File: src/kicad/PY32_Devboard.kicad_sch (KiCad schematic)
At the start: 19 parts, among them J2 Micro_SD_Card, J5 Conn_01x09, J6 Conn_01x09, SW1 RESET, SW2 BOOT, SW3 RESET, SW4 BOOT, U1 CH340N, U2 ME6211A33M3G-N, U3 PY32F002BF15P6TR

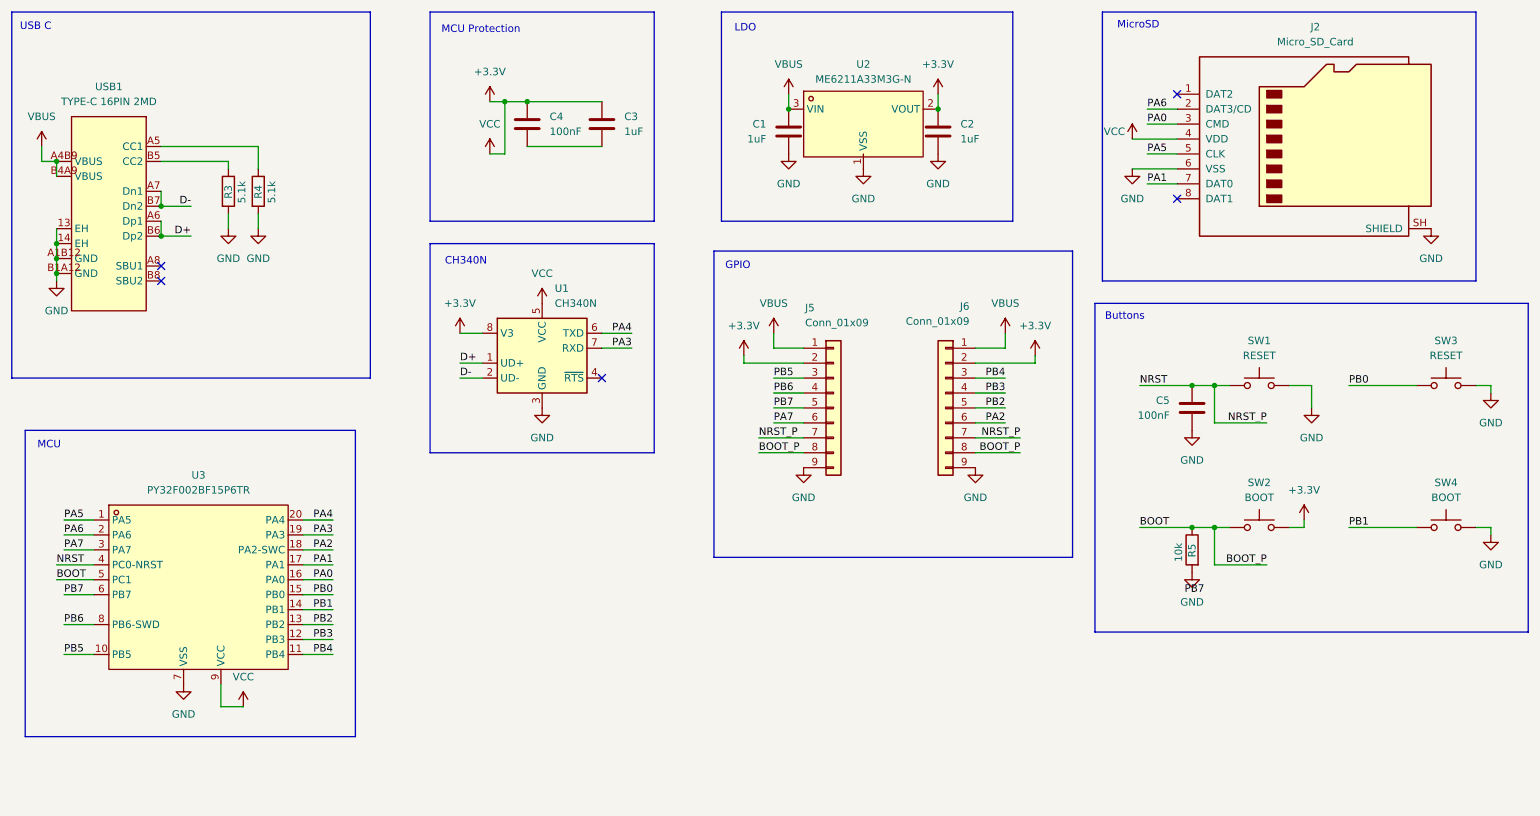
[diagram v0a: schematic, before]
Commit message: Changed Github For Fixed PCB
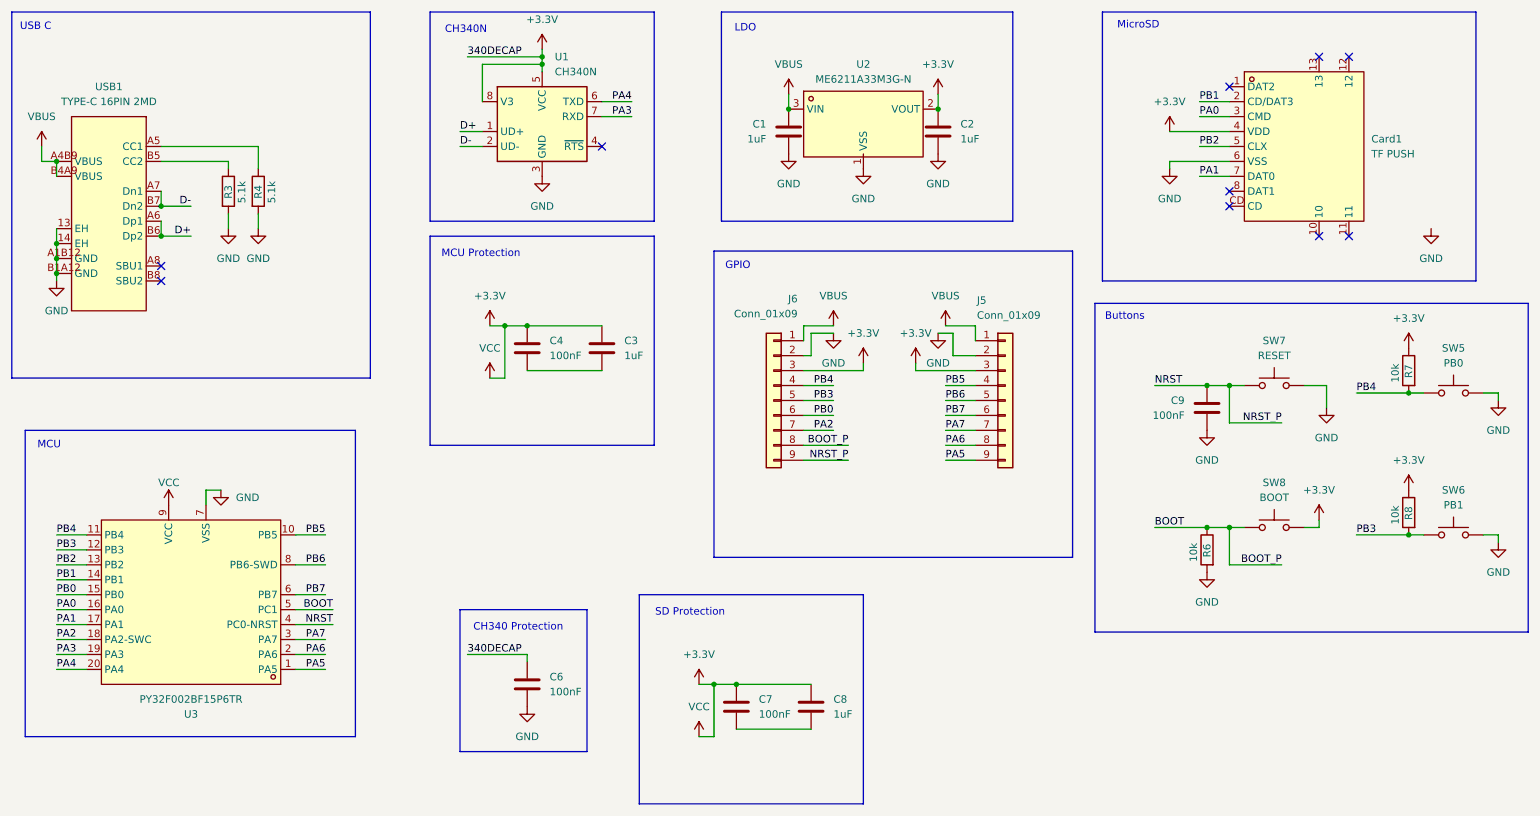
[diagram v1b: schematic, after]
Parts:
- removed C5: 100nF, Capacitor_SMD:C_0805_2012Metric, symbol Device:C
- removed J2: Micro_SD_Card, easyeda2kicad:TF-SMD_TF-PUSH, symbol Connector:Micro_SD_Card
- removed R5: 10k, Resistor_SMD:R_0805_2012Metric, symbol Device:R
- removed SW1, SW3: RESET, easyeda2kicad:SW-SMD_L3.9-W3.0-P4.45, symbol Switch:SW_Push
- removed SW2, SW4: BOOT, easyeda2kicad:SW-SMD_L3.9-W3.0-P4.45, symbol Switch:SW_Push
- added C6, C7, C9: 100nF, Capacitor_SMD:C_0805_2012Metric, symbol Device:C
- added C8: 1uF, Capacitor_SMD:C_0805_2012Metric, symbol Device:C
- added Card1: TF PUSH, easyeda2kicad:TF-SMD_TF-PUSH, symbol easyeda2kicad:TFPUSH
- added R6, R7, R8: 10k, Resistor_SMD:R_0805_2012Metric, symbol Device:R
- added SW5: PB0, easyeda2kicad:SW-SMD_L3.9-W3.0-P4.45, symbol Switch:SW_Push
- added SW6: PB1, easyeda2kicad:SW-SMD_L3.9-W3.0-P4.45, symbol Switch:SW_Push
- added SW7: RESET, easyeda2kicad:SW-SMD_L3.9-W3.0-P4.45, symbol Switch:SW_Push
- added SW8: BOOT, easyeda2kicad:SW-SMD_L3.9-W3.0-P4.45, symbol Switch:SW_Push
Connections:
- net +3.3V: now also J5.3 (Pin_3), J6.3 (Pin_3), C6.1, C7.1, C8.1, Card1.4 (VDD), R7.1, R8.1, SW8.2; no longer J5.2 (Pin_2), J6.2 (Pin_2)
- net BOOT: now also R6.1, SW8.1; no longer J5.8 (Pin_8)
- net GND: now also J5.2 (Pin_2), J6.2 (Pin_2), C6.2, C9.2, Card1.6 (VSS), R6.2, SW5.2, SW6.2, SW7.2; no longer J5.9 (Pin_9), J6.9 (Pin_9)
- net NRST: now also J6.9 (Pin_9), C9.1, SW7.1; no longer J5.7 (Pin_7), J6.7 (Pin_7)
- net PA0: now also Card1.3 (CMD)
- net PA1: now also Card1.7 (DAT0)
- net PA2: now also J6.7 (Pin_7); no longer J6.6 (Pin_6)
- net PA5: now also J5.9 (Pin_9)
- net PA6: now also J5.8 (Pin_8)
- net PA7: now also J5.7 (Pin_7); no longer J5.6 (Pin_6)
- net PB0: now also J6.6 (Pin_6)
- net PB1: now also Card1.2 (CD/DAT3)
- net PB2: now also Card1.5 (CLX); no longer J6.5 (Pin_5)
- net PB3: now also J6.5 (Pin_5), R8.2, SW6.1; no longer J6.4 (Pin_4)
- net PB4: now also J6.4 (Pin_4), R7.2, SW5.1; no longer J6.3 (Pin_3)
- net PB5: now also J5.4 (Pin_4); no longer J5.3 (Pin_3)
- net PB6: now also J5.5 (Pin_5); no longer J5.4 (Pin_4)
- net PB7: now also J5.6 (Pin_6); no longer J5.5 (Pin_5)
- new net: C7.2, C8.2
- no-connect marks 5 -> 10
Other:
- note added: "CH340 Protection"
- note added: "SD Protection"
- moved on the sheet: C3, C4, J5, J6, U1, U3
